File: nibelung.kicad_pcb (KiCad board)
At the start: 2 copper layers, 35.6 x 35.6 mm, 53 parts, among them J1 JST_SH_01x03, J2 AudioJack3-TSW, J3 ScrewTerm_01x08_2.54mm, J4 ScrewTerm_01x08_2.54mm, J5 JST_SH_01x03, J6 JST_SH_01x03, U1 74HCT245, U2 LTC2850xS8, U3 MIC5219-5.0YM5, U4 ADP122AUJZ-3.3

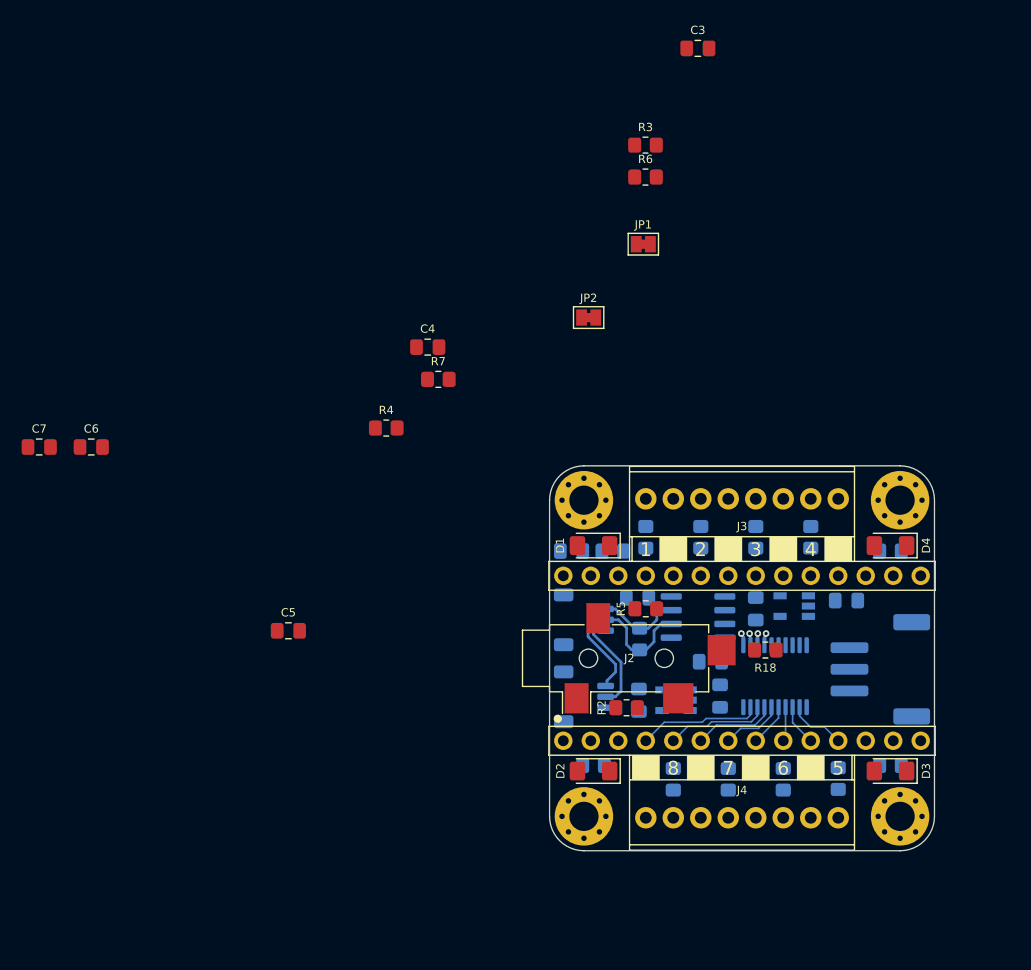
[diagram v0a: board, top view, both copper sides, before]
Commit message: Add right angle pushbuttons
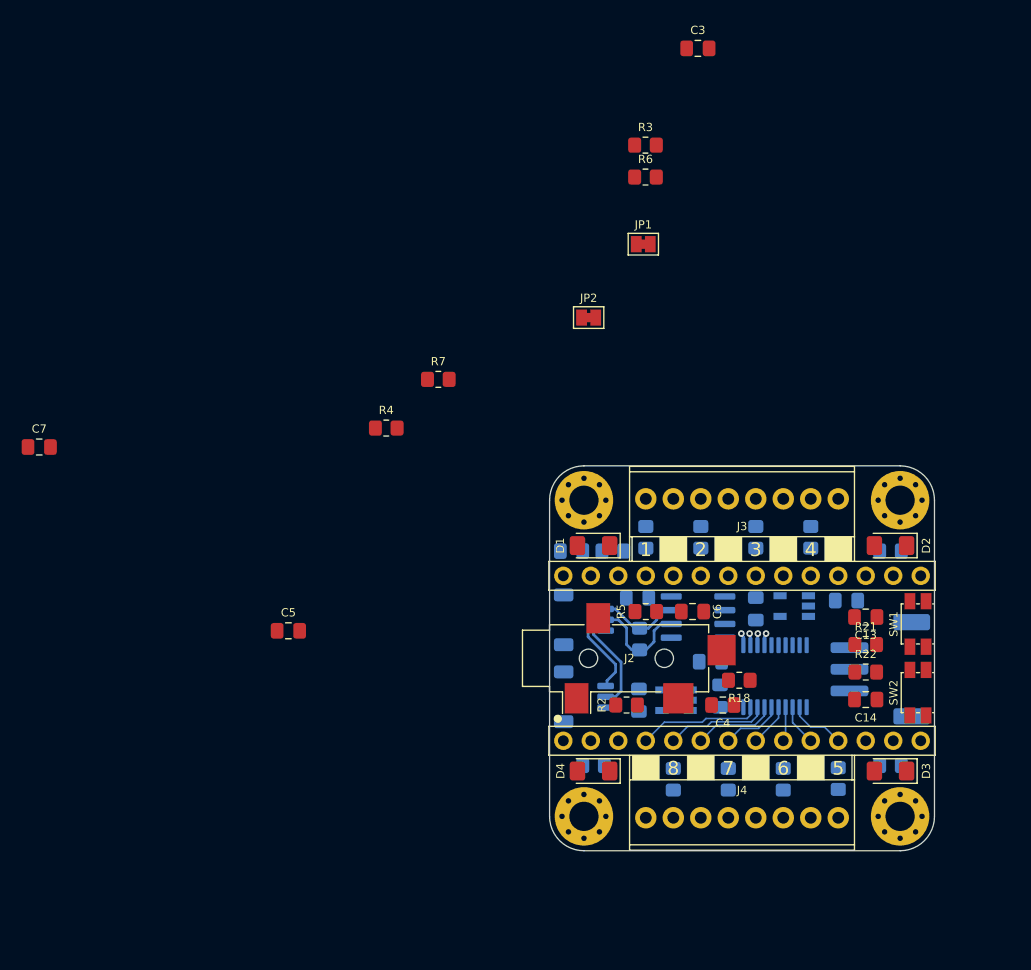
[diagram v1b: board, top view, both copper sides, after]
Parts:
- added C13: 0.1uF, Capacitor_SMD:C_0805_2012Metric_Pad1.18x1.45mm_HandSolder, F.Cu at (132.1, 97.8)
- added C14: 0.1uF, Capacitor_SMD:C_0805_2012Metric_Pad1.18x1.45mm_HandSolder, F.Cu at (132.1, 105.4)
- added R21: 10k, Resistor_SMD:R_0805_2012Metric_Pad1.20x1.40mm_HandSolder, F.Cu at (132.1, 100.3)
- added R22: 10k, Resistor_SMD:R_0805_2012Metric_Pad1.20x1.40mm_HandSolder, F.Cu at (132.1, 102.9)
- added SW1: PTS840 GK, nibelung:SW_Push_1P1T_NO_CK_PTS840, F.Cu at (136.9, 98.4)
- added SW2: PTS840 GK, nibelung:SW_Push_1P1T_NO_CK_PTS840, F.Cu at (136.9, 104.8)
- J1: value JST_SH_01x03 -> JST_PH_01x03
- moved C6 57.6 mm to (116.1, 97.3), turned to 180 degrees
- moved C4 42.9 mm to (118.9, 105.9), turned to 180 degrees
- moved R18 3.69 mm to (120.4, 103.6)
- moved R2 0.25 mm to (110.0, 105.9)
- moved R5 0.25 mm to (111.8, 97.3), turned to 180 degrees
- renumbered D4 to D2, D2 to D4
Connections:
- net /IND1 renamed /INDC
- net /IND2 renamed /INDB
- net /IND3 renamed /INDA
- A1 pad 26: Net-(A1-Pad26) -> +3V3A
- R3 pad 1: +3V3 -> +3V3A
- R6 pad 1: +3V3 -> +3V3A

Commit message: Continue placement
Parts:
- removed JP1, JP2: SJ2, Jumper:SolderJumper-2_P1.3mm_Bridged_Pad1.0x1.5mm
- C13, C14, R21, R22, SW1, SW2: moved to B.Cu
- J1: moved to F.Cu
- R1: value 100 -> 120
- moved C7 71.4 mm to (125.0, 99.3)
- moved R3 52.2 mm to (121.7, 105.4), turned to 270 degrees
- moved C5 46.8 mm to (125.0, 106.2)
- moved R6 45.6 mm to (121.7, 101.6), turned to 90 degrees
- moved R4 44.0 mm to (125.0, 103.9)
- moved R7 41.4 mm to (125.0, 101.6)
- moved C3 34.7 mm to (119.9, 79.8)
- moved R18 6.62 mm to (119.9, 97.0), turned to 0 degrees
- moved C13 1.27 mm to (133.1, 97.0), turned to 90 degrees
- moved C10 1.09 mm to (122.3, 96.0), turned to 180 degrees
- moved J1 1.02 mm to (133.4, 101.6), turned to 90 degrees
- moved U3 1.02 mm to (126.5, 96.8)
- moved C9 0.92 mm to (129.8, 97.0), turned to 270 degrees
- moved C6 0.57 mm to (115.6, 97.0)
- moved R5 0.57 mm to (111.3, 97.0)
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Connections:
- net /A renamed /D+
- net /B renamed /D-
- net /CS renamed Net-(A1-Pad12)
- net /MISO renamed Net-(A1-Pad14)
- net /MOSI renamed Net-(A1-Pad13)
- net /SCK renamed Net-(A1-Pad15)
- A1 pad 2: Net-(A1-Pad2) -> /INDC
- A1 pad 21: Net-(A1-Pad21) -> /INDA
- A1 pad 3: Net-(A1-Pad3) -> /INDB
- R18 pad 1: +3V3 -> +3V3A
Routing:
- net +3V3A: track 0.00 -> 25.2 mm
- net /AUD_R: track 0.00 -> 8.39 mm
- net /AUD_L: track 0.00 -> 7.07 mm
- net /AUD_L_ADC: track 0.00 -> 5.91 mm
- net /AUD_R_ADC: track 0.00 -> 5.02 mm
- net /D-: track 17.5 -> 19.9 mm
- net /D+: track 20.1 -> 20.9 mm
- added copper zone on F.Cu, net GND
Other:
- net class RS-485 added: clearance 0.1524, trace_width 0.2032, via_dia 0.6096, via_drill 0.3048
- board text added: "DATA"
- board text removed: "RS485"

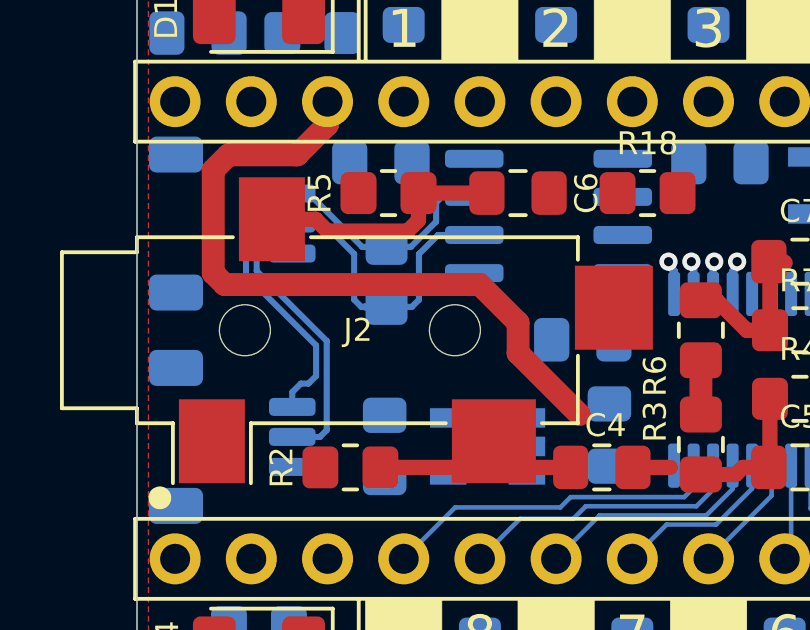
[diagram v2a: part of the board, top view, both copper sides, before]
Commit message: Length-match differential pair traces
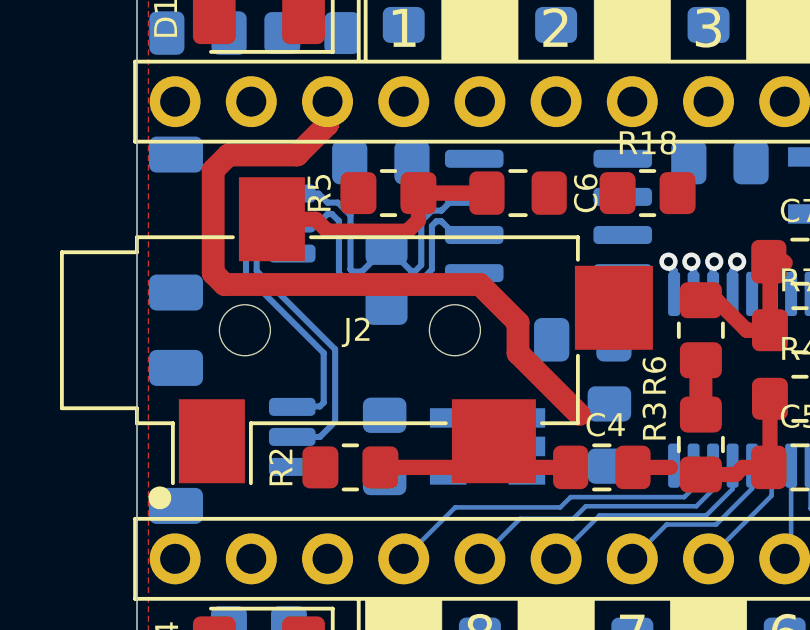
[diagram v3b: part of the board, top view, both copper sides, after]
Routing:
- net /D-: track 19.9 -> 21.1 mm

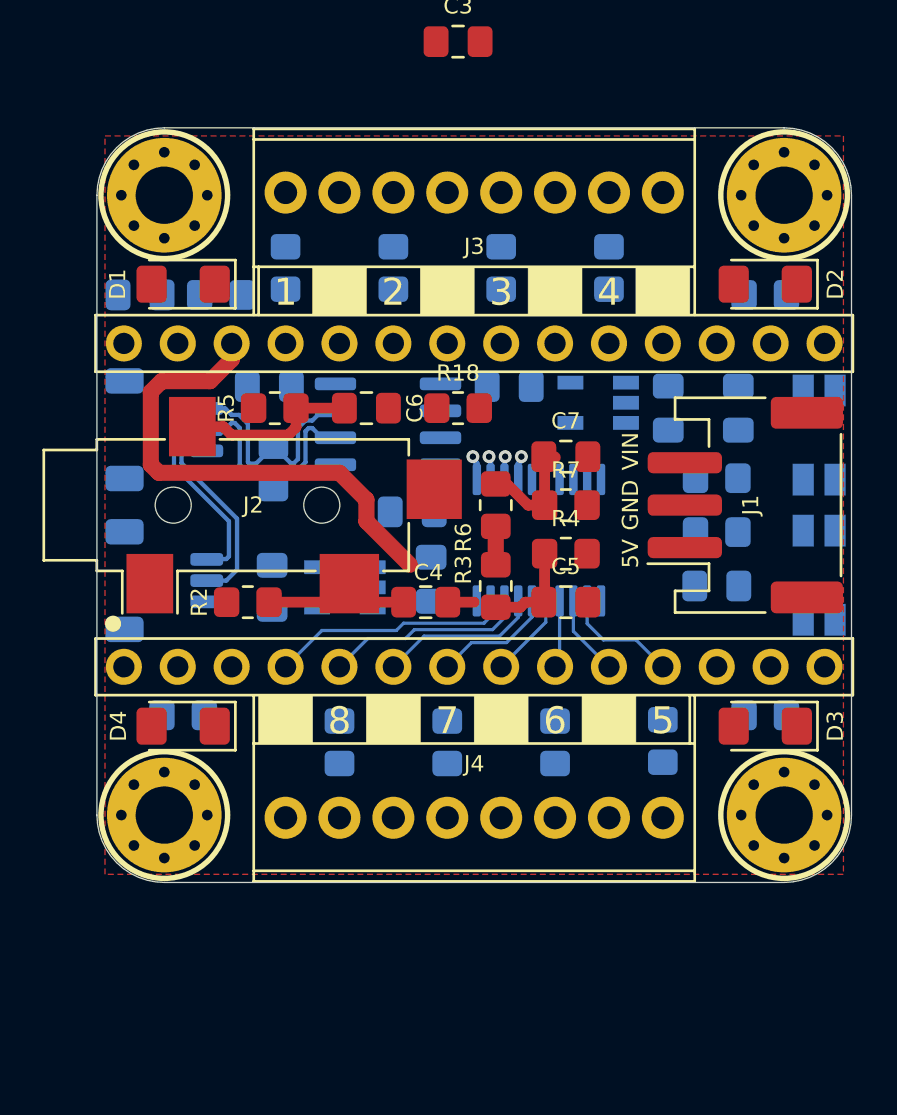
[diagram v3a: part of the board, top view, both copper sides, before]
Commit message: Replace 2.54mm pitch terminals with 3.5mm pitch ones
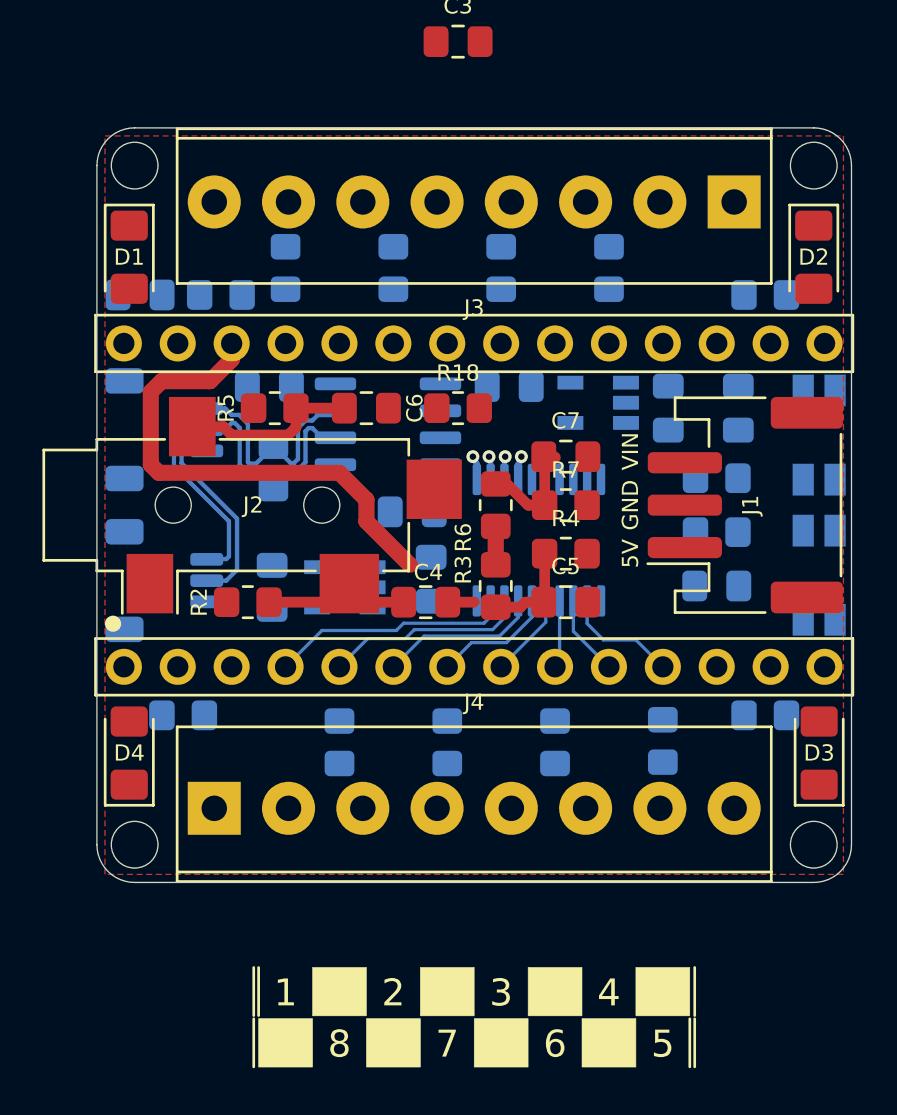
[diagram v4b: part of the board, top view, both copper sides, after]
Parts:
- H1, H2, H3, H4: value M2.5 -> M2; footprint MountingHole:MountingHole_2.7mm_M2.5_Pad_Via -> MountingHole:MountingHole_2.2mm_M2
- J3, J4: footprint nibelung:TerminalBlock_Molex_397730008_1x08_P2.54mm_Horizontal -> nibelung:TerminalBlock_Molex_393570008_1x08_P3.50mm_Horizontal
- moved J3 3.39 mm to (132.9, 87.3)
- moved J4 3.39 mm to (108.4, 115.9)
- moved D1 2.84 mm to (104.4, 89.9), turned to 270 degrees
- moved D3 2.84 mm to (136.9, 113.3), turned to 90 degrees
- moved D4 2.84 mm to (104.4, 113.3), turned to 90 degrees
- moved D2 2.62 mm to (136.7, 89.9), turned to 270 degrees
- moved H1 1.98 mm to (104.6, 85.6)
- moved H3 1.98 mm to (104.6, 117.6)
- moved H2 1.98 mm to (136.7, 85.6)
- moved H4 1.98 mm to (136.7, 117.6)
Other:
- outline, holes or cut-outs redrawn

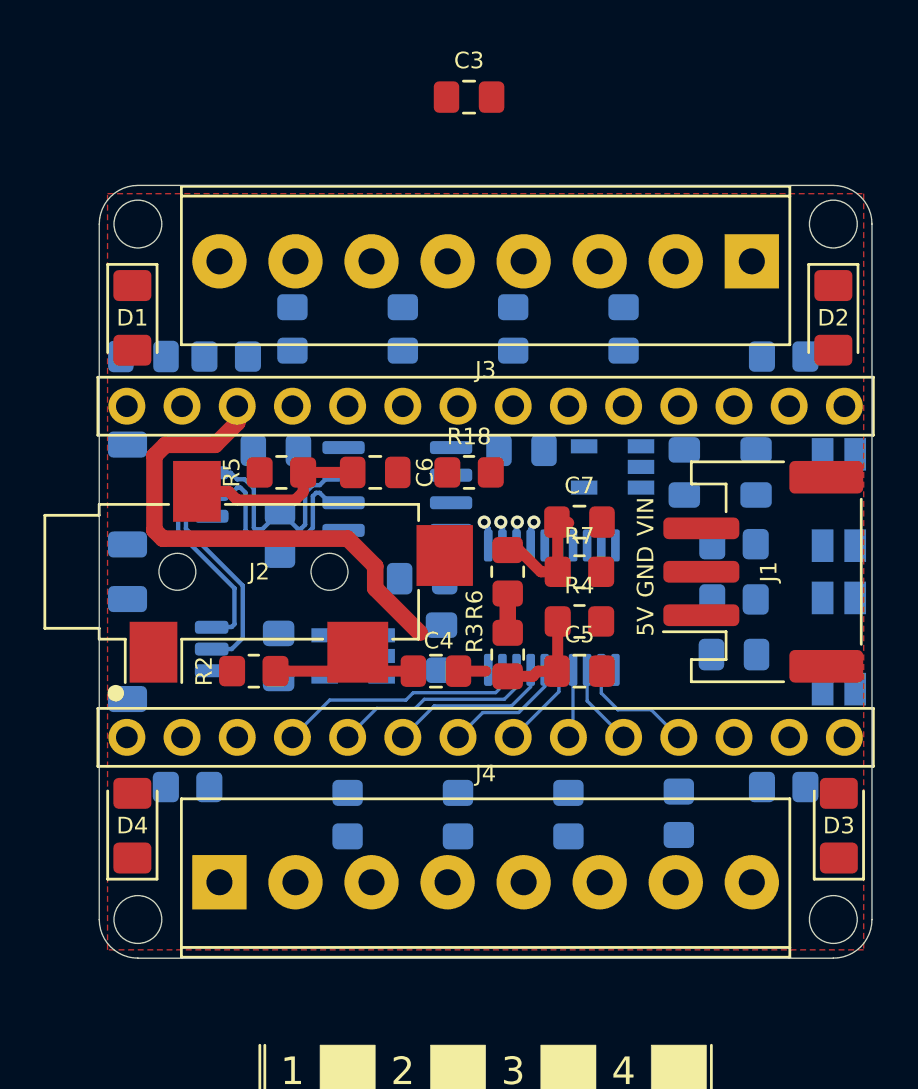
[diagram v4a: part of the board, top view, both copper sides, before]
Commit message: Make board less wide
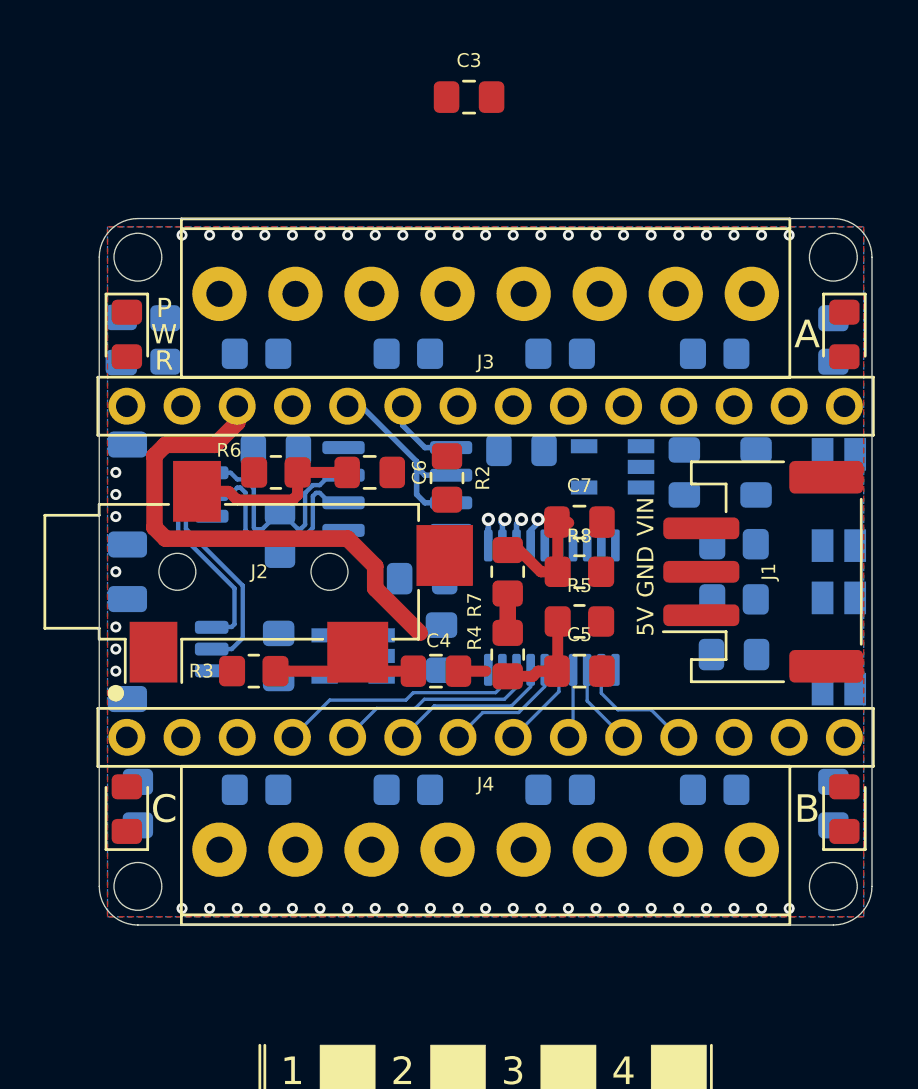
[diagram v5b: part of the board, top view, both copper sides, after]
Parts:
- D1, D2, D3, D4: footprint LED_SMD:LED_1206_3216Metric_Pad1.42x1.75mm_HandSolder -> LED_SMD:LED_0805_2012Metric_Pad1.15x1.40mm_HandSolder
- moved R13 4.34 mm to (110.1, 111.6), turned to 180 degrees
- moved R17 4.34 mm to (131.2, 91.6), turned to 0 degrees
- moved R9 2.90 mm to (105.9, 90.9), turned to 90 degrees
- moved R14 2.56 mm to (117.1, 111.6), turned to 180 degrees
- moved R18 2.44 mm to (124.1, 91.6), turned to 0 degrees
- moved R12 2.41 mm to (104.6, 112.3), turned to 90 degrees
- moved R10 2.41 mm to (136.7, 90.9), turned to 270 degrees
- moved R11 2.41 mm to (136.7, 112.3), turned to 90 degrees
- moved R20 2.01 mm to (110.1, 91.6), turned to 0 degrees
- moved R16 1.97 mm to (131.2, 111.6), turned to 180 degrees
- moved H1 1.52 mm to (104.6, 87.1)
- moved H2 1.52 mm to (136.7, 87.1)
- moved H3 1.52 mm to (104.6, 116.1)
- moved H4 1.52 mm to (136.7, 116.1)
- moved J3 1.50 mm to (132.9, 88.8)
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- renumbered R20 to R10, R19 to R11, R9 to R12, R10 to R13, R11 to R14, R12 to R15, R13 to R16, R14 to R17, R15 to R18, R16 to R19, R18 to R2, R17 to R20, R2 to R3, R3 to R4, R4 to R5, R5 to R6, R6 to R7, R7 to R8, R8 to R9
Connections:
- net Net-(A1-Pad22) renamed /DASH_TX
- A1 pad 18: /RX -> /UART_RX
- A1 pad 19: /TX -> /UART_TX
- A1 pad 20: /TXEN -> /AUD_DET
- A1 pad 23: Net-(A1-Pad23) -> /DASH_RX
- A1 pad 24: Net-(A1-Pad24) -> /DASH_TXEN
- U2 pad 1: /RX -> /DASH_RX
- U2 pad 2: /TXEN -> /DASH_TXEN
- U2 pad 3: /TXEN -> /DASH_TXEN
- U2 pad 4: /TX -> /DASHTX
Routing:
- net /DASH_TXEN: track 0.00 -> 9.24 mm
- net /DASH_RX: track 0.00 -> 3.53 mm
- net GND: vias 0 -> 53
- added copper zone on B.Cu, net GND
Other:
- board size 35.6 x 35.6 mm -> 35.6 x 32.5 mm
- board text added: "C"
- board text added: "DASH"
- board text added: "P"
- board text added: "R"
- board text added: "W"
- board text removed: "DATA"
